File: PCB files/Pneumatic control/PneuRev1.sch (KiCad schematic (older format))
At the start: 5 parts

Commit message: 11/29 OpAmp switching
-Changed circuit from High side switch IC to opamp symbol
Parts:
- removed C?: C, symbol C
- removed R? (x3): R, symbol R
- removed U?: TPS1H000AQDGNRQ1, symbol TPS1H000AQDGNRQ1
- added R?: 1k, symbol R
- added R?: 100, symbol R
- added R?: 380, symbol R
- added U?: OP07, symbol OP07
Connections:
- net labels removed: +24V
- wire segments 15 -> 11
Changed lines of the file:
@@
 LIBS:contrib
 LIBS:valves
+LIBS:PneuRev1-cache
 EELAYER 25 0
 EELAYER END
@@
 $EndDescr
 $Comp
-L TPS1H000AQDGNRQ1 U?
-U 1 1 5BECF8AF
-P 6100 3725
-F 0 "U?" H 6100 3225 60  0000 C CNN
-F 1 "TPS1H000AQDGNRQ1" H 6100 4375 60  0000 C CNN
-F 2 "" H 6100 3725 60  0001 C CNN
-F 3 "" H 6100 3725 60  0001 C CNN
-	1    6100 3725
+L +5V #PWR?
+U 1 1 5BED02C0
+P 4375 2925
+F 0 "#PWR?" H 4375 2775 50  0001 C CNN
+F 1 "+5V" H 4375 3065 50  0000 C CNN
+F 2 "" H 4375 2925 50  0001 C CNN
+F 3 "" H 4375 2925 50  0001 C CNN
+	1    4375 2925
+	1    0    0    -1
+$EndComp
+$Comp
+L OP07 U?
+U 1 1 5C00B50F
+P 5600 3375
+F 0 "U?" H 5650 3625 50  0000 L CNN
+F 1 "OP07" H 5650 3525 50  0000 L CNN
+F 2 "" H 5650 3425 50  0001 C CNN
+F 3 "" H 5650 3525 50  0001 C CNN
+	1    5600 3375
+	1    0    0    -1
+$EndComp
+Wire Wire Line
+	4375 2925 4375 3275
+Wire Wire Line
+	4375 3275 5300 3275
+$Comp
+L R R?
+U 1 1 5C00B58E
+P 4375 3425
+F 0 "R?" V 4455 3425 50  0000 C CNN
+F 1 "1k" V 4375 3425 50  0000 C CNN
+F 2 "" V 4305 3425 50  0001 C CNN
+F 3 "" H 4375 3425 50  0001 C CNN
+	1    4375 3425
+	1    0    0    -1
+$EndComp
+$Comp
+L GND #PWR?
+U 1 1 5C00B5C1
+P 4375 3575
+F 0 "#PWR?" H 4375 3325 50  0001 C CNN
+F 1 "GND" H 4375 3425 50  0000 C CNN
+F 2 "" H 4375 3575 50  0001 C CNN
+F 3 "" H 4375 3575 50  0001 C CNN
+	1    4375 3575
+	1    0    0    -1
+$EndComp
+Wire Wire Line
+	5150 3475 5150 4025
+Wire Wire Line
+	5150 3475 5300 3475
+$Comp
+L R R?
+U 1 1 5C00B637
+P 5150 4175
+F 0 "R?" V 5230 4175 50  0000 C CNN
+F 1 "100" V 5150 4175 50  0000 C CNN
+F 2 "" V 5080 4175 50  0001 C CNN
+F 3 "" H 5150 4175 50  0001 C CNN
+	1    5150 4175
 	1    0    0    -1
 $EndComp
 $Comp
 L R R?
-U 1 1 5BECF8E3
-P 4675 3325
-F 0 "R?" V 4755 3325 50  0000 C CNN
-F 1 "R" V 4675 3325 50  0000 C CNN
-F 2 "" V 4605 3325 50  0001 C CNN
-F 3 "" H 4675 3325 50  0001 C CNN
-	1    4675 3325
+U 1 1 5C00B68B
+P 5550 3950
+F 0 "R?" V 5630 3950 50  0000 C CNN
+F 1 "380" V 5550 3950 50  0000 C CNN
+F 2 "" V 5480 3950 50  0001 C CNN
+F 3 "" H 5550 3950 50  0001 C CNN
+	1    5550 3950
 	0    1    1    0
 $EndComp
-$Comp
-L R R?
-U 1 1 5BECF983
-P 5050 4075
-F 0 "R?" V 5130 4075 50  0000 C CNN
-F 1 "R" V 5050 4075 50  0000 C CNN
-F 2 "" V 4980 4075 50  0001 C CNN
-F 3 "" H 5050 4075 50  0001 C CNN
-	1    5050 4075
-	0    1    1    0
-$EndComp
-$Comp
-L C C?
-U 1 1 5BECFA51
-P 6900 4075
-F 0 "C?" H 6925 4175 50  0000 L CNN
-F 1 "C" H 6925 3975 50  0000 L CNN
-F 2 "" H 6938 3925 50  0001 C CNN
-F 3 "" H 6900 4075 50  0001 C CNN
-	1    6900 4075
-	-1   0    0    1
-$EndComp
+Wire Wire Line
+	5150 3950 5400 3950
+Connection ~ 5150 3950
+Wire Wire Line
+	5700 3950 6050 3950
+Wire Wire Line
+	6050 3950 6050 3375
+Wire Wire Line
+	5900 3375 6750 3375
+Wire Wire Line
+	5500 3075 5500 2725
 $Comp
 L GND #PWR?
-U 1 1 5BECFB91
-P 6900 4475
-F 0 "#PWR?" H 6900 4225 50  0001 C CNN
-F 1 "GND" H 6900 4325 50  0000 C CNN
-F 2 "" H 6900 4475 50  0001 C CNN
-F 3 "" H 6900 4475 50  0001 C CNN
-	1    6900 4475
-	1    0    0    -1
-$EndComp
-$Comp
-L R R?
-U 1 1 5BECFDE5
-P 5025 3525
-F 0 "R?" V 5105 3525 50  0000 C CNN
-F 1 "R" V 5025 3525 50  0000 C CNN
-F 2 "" V 4955 3525 50  0001 C CNN
-F 3 "" H 5025 3525 50  0001 C CNN
-	1    5025 3525
-	-1   0    0    1
-$EndComp
-$Comp
-L GND #PWR?
-U 1 1 5BECFE76
-P 5025 3675
-F 0 "#PWR?" H 5025 3425 50  0001 C CNN
-F 1 "GND" H 5025 3525 50  0000 C CNN
-F 2 "" H 5025 3675 50  0001 C CNN
-F 3 "" H 5025 3675 50  0001 C CNN
-	1    5025 3675
-	1    0    0    -1
-$EndComp
-$Comp
-L +24V #PWR?
-U 1 1 5BED01EB
-P 6900 3050
-F 0 "#PWR?" H 6900 2900 50  0001 C CNN
-F 1 "+24V" H 6900 3190 50  0000 C CNN
-F 2 "" H 6900 3050 50  0001 C CNN
-F 3 "" H 6900 3050 50  0001 C CNN
-	1    6900 3050
+U 1 1 5C00B76C
+P 5500 3700
+F 0 "#PWR?" H 5500 3450 50  0001 C CNN
+F 1 "GND" H 5500 3550 50  0000 C CNN
+F 2 "" H 5500 3700 50  0001 C CNN
+F 3 "" H 5500 3700 50  0001 C CNN
+	1    5500 3700
 	1    0    0    -1
 $EndComp
 Wire Wire Line
-	4825 3325 5550 3325
-Wire Wire Line
-	5200 3925 5550 3925
-Wire Wire Line
-	6650 3925 6900 3925
-Wire Wire Line
-	6900 4225 6900 4475
-Wire Wire Line
-	5025 3375 5025 3325
-Connection ~ 5025 3325
-Wire Wire Line
-	5200 3925 5200 4075
-Wire Wire Line
-	6900 3050 6900 3325
-Wire Wire Line
-	6900 3325 6650 3325
+	5500 3675 5500 3700
 $Comp
-L +5V #PWR?
-U 1 1 5BED02C0
-P 4125 3125
-F 0 "#PWR?" H 4125 2975 50  0001 C CNN
-F 1 "+5V" H 4125 3265 50  0000 C CNN
-F 2 "" H 4125 3125 50  0001 C CNN
-F 3 "" H 4125 3125 50  0001 C CNN
-	1    4125 3125
+L GND #PWR?
+U 1 1 5C00B92E
+P 5150 4525
+F 0 "#PWR?" H 5150 4275 50  0001 C CNN
+F 1 "GND" H 5150 4375 50  0000 C CNN
+F 2 "" H 5150 4525 50  0001 C CNN
+F 3 "" H 5150 4525 50  0001 C CNN
+	1    5150 4525
 	1    0    0    -1
 $EndComp
 Wire Wire Line
-	4125 3125 4125 3325
-Wire Wire Line
-	4125 3325 4525 3325
-Wire Wire Line
-	6650 3725 7200 3725
-Wire Wire Line
-	7200 3725 7200 4425
-Wire Wire Line
-	7200 4425 6900 4425
-Connection ~ 6900 4425
-$Comp
-L GND #PWR?
-U 1 1 5BED065C
-P 4775 4500
-F 0 "#PWR?" H 4775 4250 50  0001 C CNN
-F 1 "GND" H 4775 4350 50  0000 C CNN
-F 2 "" H 4775 4500 50  0001 C CNN
-F 3 "" H 4775 4500 50  0001 C CNN
-	1    4775 4500
-	1    0    0    -1
-$EndComp
-Wire Wire Line
-	4900 4075 4775 4075
-Wire Wire Line
-	4775 4075 4775 4500
+	5150 4325 5150 4525
+Connection ~ 6050 3375
 $EndSCHEMATC

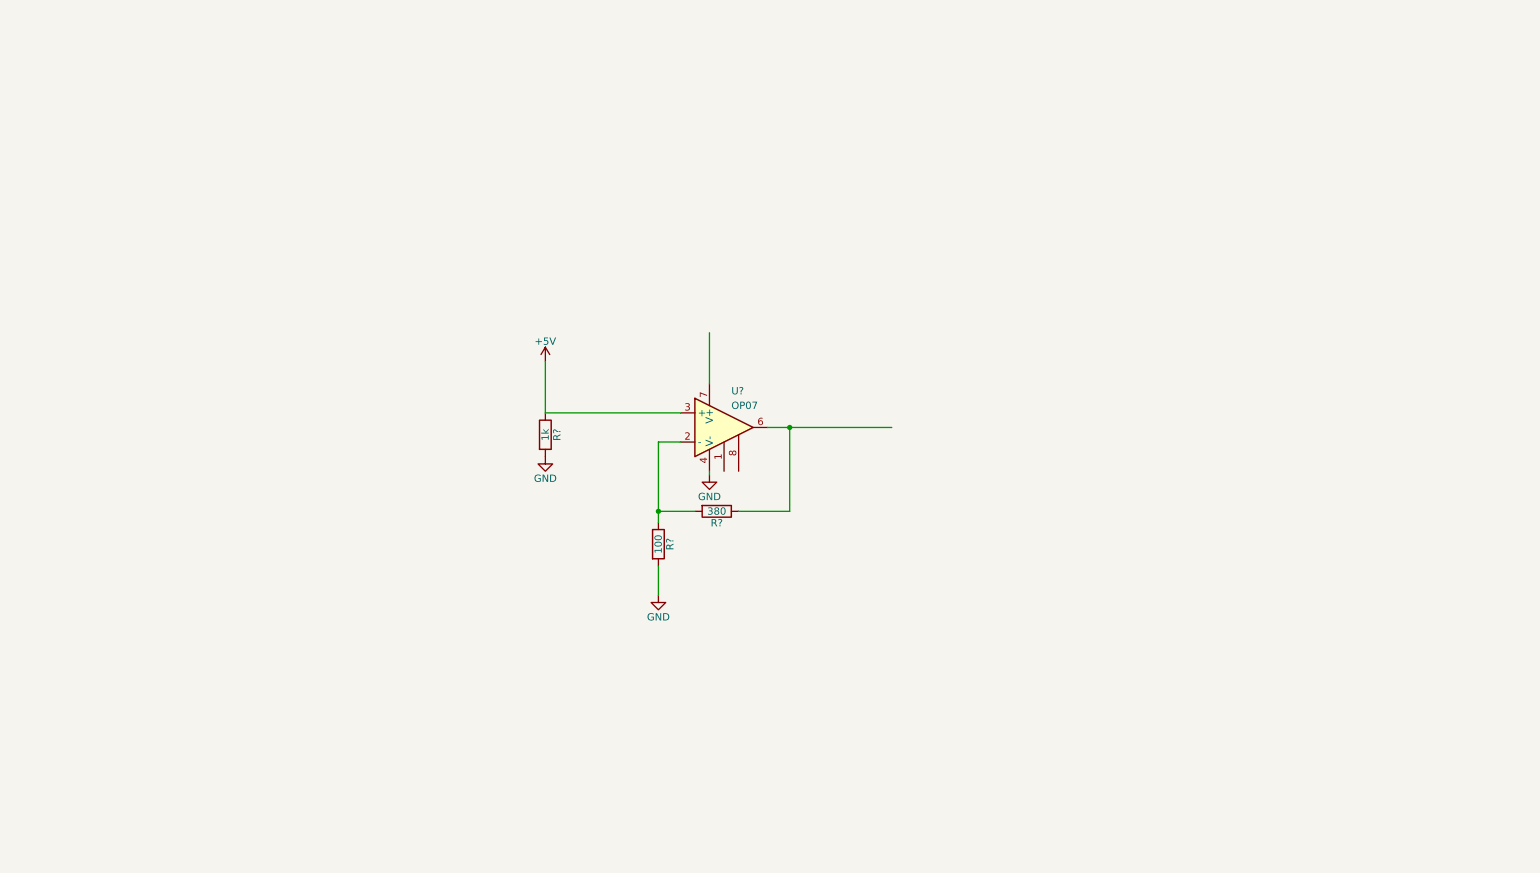
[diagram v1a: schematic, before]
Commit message: 11/30/2018
-Added bus lines
-Added net names for in/out
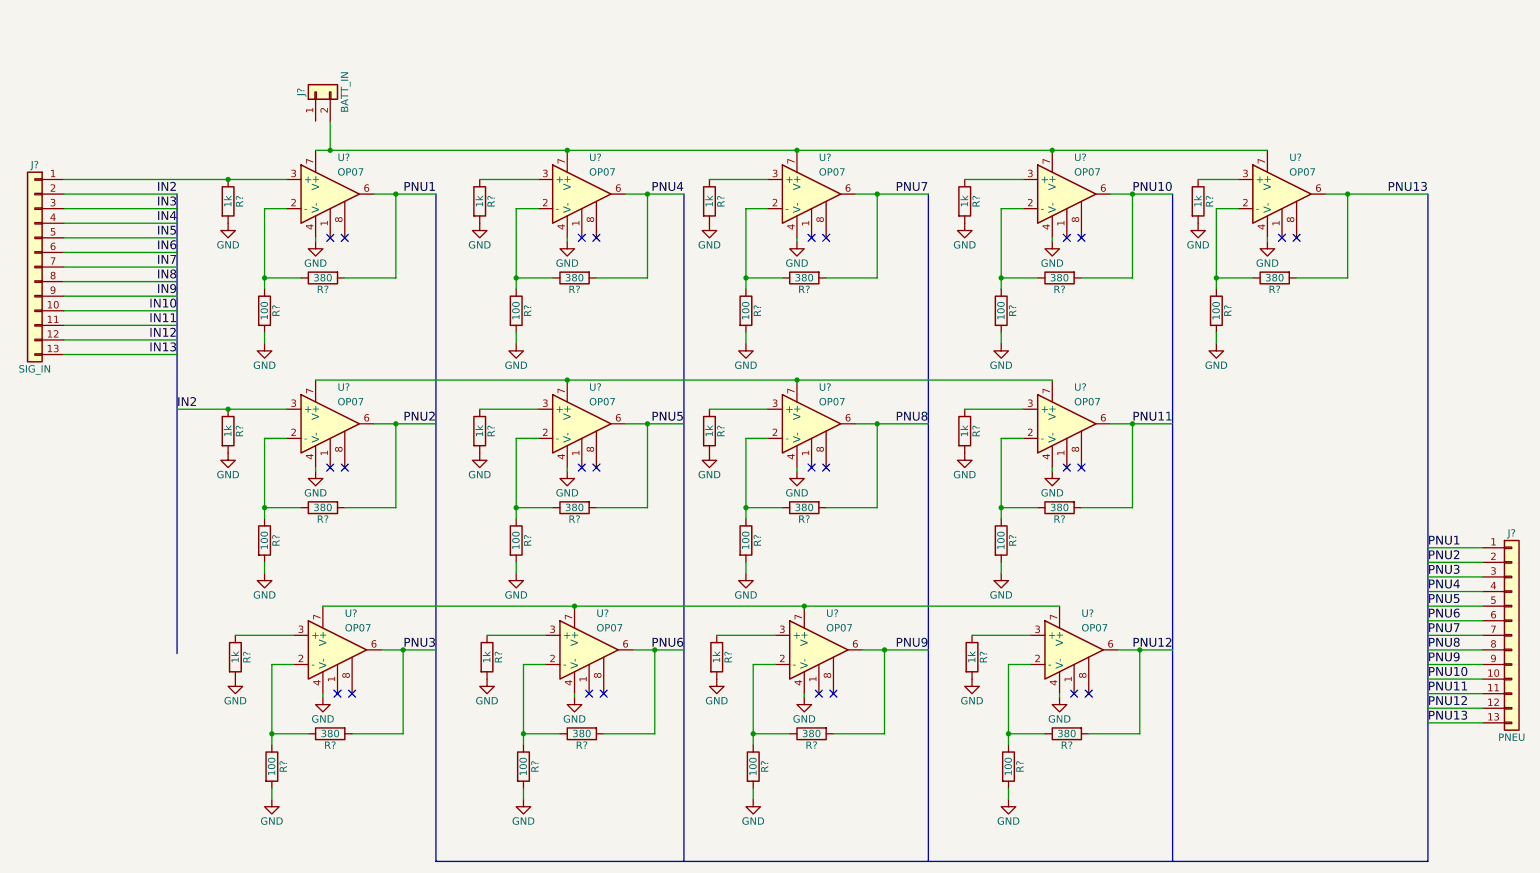
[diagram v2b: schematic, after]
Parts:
- added J?: SIG_IN, symbol Conn_01x13
- added J?: PNEU, symbol Conn_01x13
- added J?: BATT_IN, symbol Conn_01x02
- added R? (x12): 1k, symbol R
- added R? (x12): 100, symbol R
- added R? (x12): 380, symbol R
- added U? (x12): OP07, symbol OP07
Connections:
- net labels added: IN10, IN11, IN12, IN13, IN2, IN3, IN4, IN5, IN6, IN7, IN8, IN9, PNU1, PNU10, PNU11, PNU12, PNU13, PNU2, PNU3, PNU4, PNU5, PNU6, PNU7, PNU8, PNU9
- net labels removed: +5V
- wire segments 11 -> 182
- no-connect marks 0 -> 26
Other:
- moved on the sheet: R?, U?

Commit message: 12/5/2018
-Changed to dual op amps
-Added ua78 regulator
-finished schematic wiring
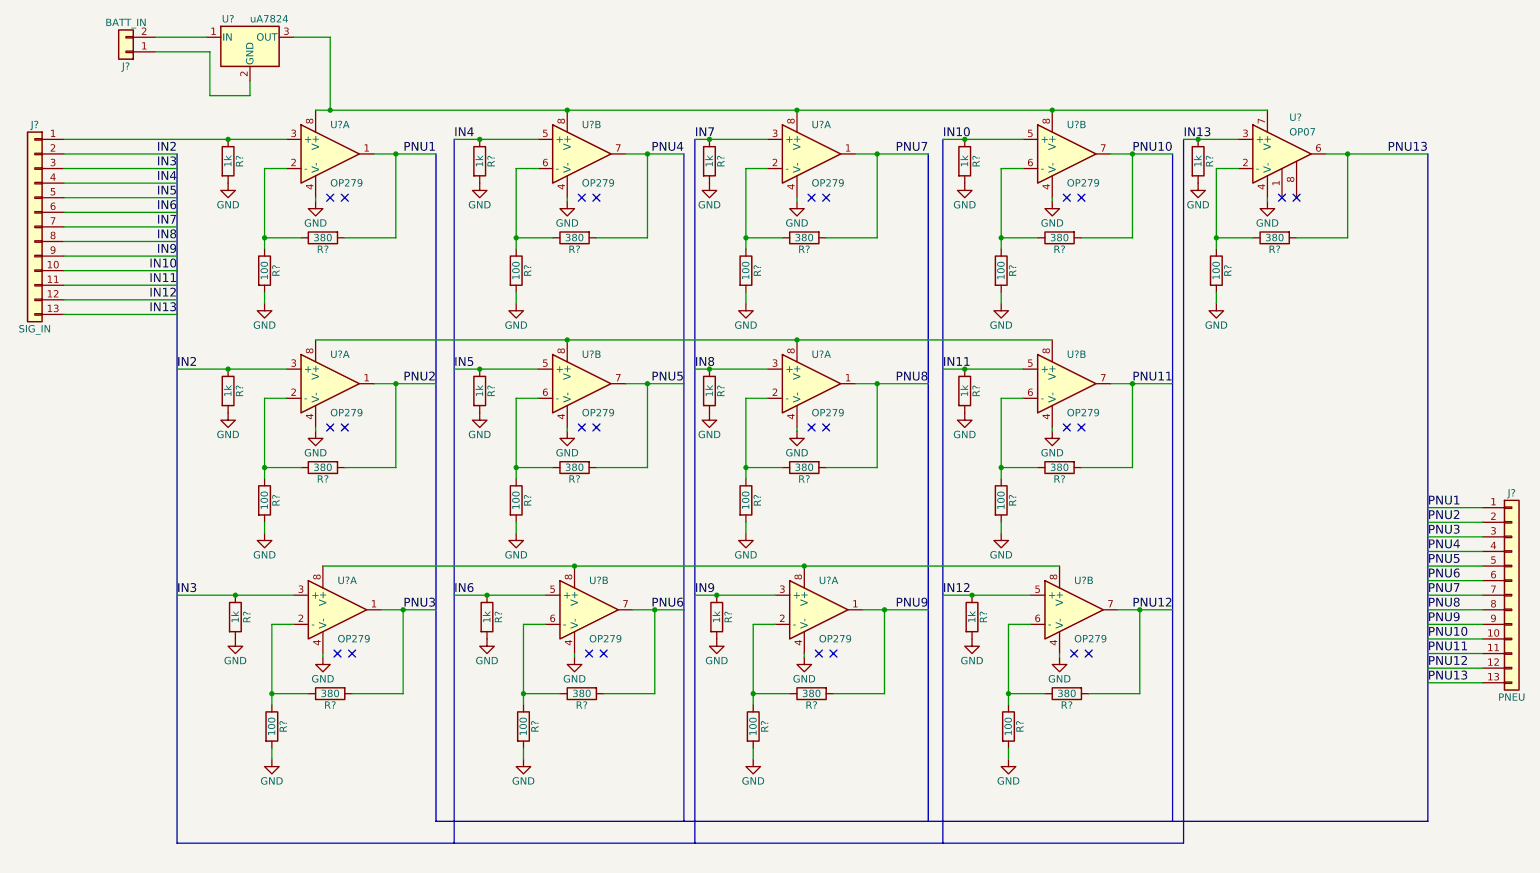
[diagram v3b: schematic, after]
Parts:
- removed U? (x12): OP07, symbol OP07
- added U? (x12): OP279, symbol OP279
- added U?: uA7824, symbol uA7824
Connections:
- net GND: now also U?.4 (V-), U?.4 (V-), U?.4 (V-), U?.4 (V-), U?.4 (V-), U?.4 (V-), U?.4 (V-), U?.4 (V-), U?.4 (V-), U?.4 (V-), U?.4 (V-), U?.4 (V-)
- net IN10: now also R?.1, U?.5 (+)
- net IN11: now also R?.1, U?.5 (+)
- net IN12: now also R?.1, U?.5 (+)
- net IN13: now also R?.1, U?.3 (+)
- net IN2: now also U?.3 (+)
- net IN3: now also R?.1, U?.3 (+)
- net IN4: now also R?.1, U?.5 (+)
- net IN5: now also R?.1, U?.5 (+)
- net IN6: now also R?.1, U?.5 (+)
- net IN7: now also R?.1, U?.3 (+)
- net IN8: now also R?.1, U?.3 (+)
- net IN9: now also R?.1, U?.3 (+)
- net PNU1: now also U?.1
- net PNU10: now also U?.7
- net PNU11: now also U?.7
- net PNU12: now also U?.7
- net PNU2: now also U?.1
- net PNU3: now also U?.1
- net PNU4: now also U?.7
- net PNU5: now also U?.7
- net PNU6: now also U?.7
- net PNU7: now also U?.1
- net PNU8: now also U?.1
- net PNU9: now also U?.1
- net at R?.1, R?.1: now also U?.2 (-) (x6)
- net at J?.1 (Pin_1), R?.1: now also U?.3 (+)
- net at J?.2 (Pin_2): now also U?.1 (IN); no longer U?.7 (V+)
- net at J?.1 (Pin_1): now also U?.2 (GND)
- net at R?.1, R?.1: now also U?.6 (-) (x6)
- new net: U?.3 (OUT), U?.7 (V+), U?.8 (V+), U?.8 (V+), U?.8 (V+), U?.8 (V+)
- new net: U?.8 (V+), U?.8 (V+), U?.8 (V+), U?.8 (V+) (x2)
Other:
- moved on the sheet: J?, R?, U?

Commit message: minor changes
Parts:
- gave numbers to parts that had none: 50
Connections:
- net IN11: now also U7.3 (+); no longer U7.5 (+)
- net IN2: now also U2.5 (+); no longer U2.3 (+)
- net IN5: now also U4.3 (+); no longer U4.5 (+)
- net IN8: now also U5.5 (+); no longer U5.3 (+)
- net PNU11: now also U7.1; no longer U7.7
- net PNU2: now also U2.7; no longer U2.1
- net PNU5: now also U4.1; no longer U4.7
- net PNU8: now also U5.7; no longer U5.1
- net at R5.1, R8.1: now also U2.6 (-); no longer U2.2 (-)
- net at R14.1, R17.1: now also U4.2 (-); no longer U4.6 (-)
- net at R23.1, R26.1: now also U5.6 (-); no longer U5.2 (-)
- net at R32.1, R35.1: now also U7.2 (-); no longer U7.6 (-)

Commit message: 1/20/2019
-Added all footprints
-Began PCB layout
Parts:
- J1, J3: footprint (none) -> Pin_Headers:Pin_Header_Straight_1x13_Pitch2.00mm
- J2: footprint (none) -> Connectors_Molex:Molex_KK-6410-02_02x2.54mm_Straight
- R1, R10, R11, R12, R13, R14, R15, R16, R17, R18, R19, R2, R20, R21, R22, R23, R24, R25, R26, R27, R28, R29, R3, R30, R31, R32, R33, R34, R35, R36, R37, R38, R39, R4, R5, R6, R7, R8, R9: footprint (none) -> Resistors_THT:R_Axial_DIN0204_L3.6mm_D1.6mm_P5.08mm_Horizontal
- U1: footprint (none) -> ua7824:TO254P1651X1067X470-3
- U2, U3, U4, U5, U6, U7, U8: footprint (none) -> dualopamp:SOIC127P600X175-8N

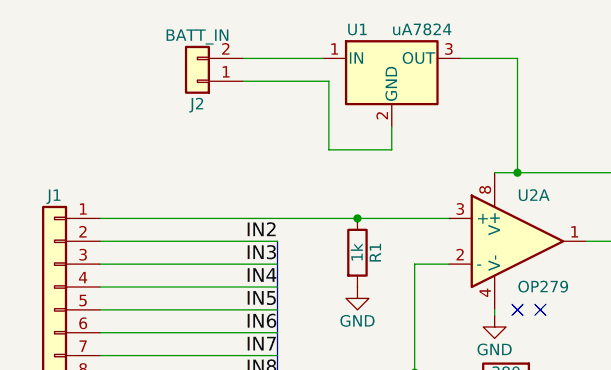
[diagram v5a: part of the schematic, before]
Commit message: 1/31/2019
-Added battery power indicator LED
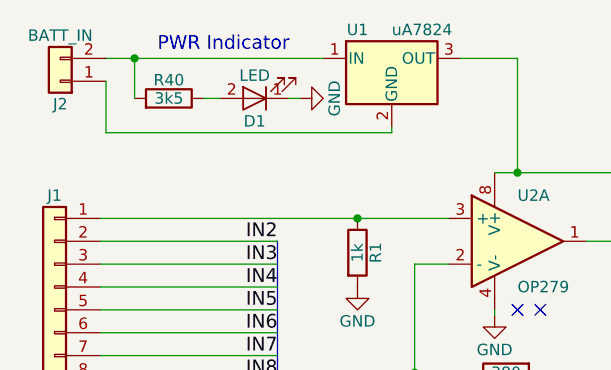
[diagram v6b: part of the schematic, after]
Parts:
- added D1: LED, LEDs:LED_D3.0mm, symbol LED
- added R40: 3k5, Resistors_THT:R_Axial_DIN0204_L3.6mm_D1.6mm_P5.08mm_Horizontal, symbol R
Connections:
- net GND: now also D1.1 (K)
- net at J2.2 (Pin_2), U1.1 (IN): now also R40.2
- new net: D1.2 (A), R40.1
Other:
- note added: "PWR Indicator"
- moved on the sheet: J2
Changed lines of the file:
@@
 L Conn_01x02 J2
 U 1 1 5C020053
-P 1500 800
-F 0 "J2" H 1500 900 50  0000 C CNN
-F 1 "BATT_IN" H 1500 600 50  0000 C CNN
-F 2 "Connectors_Molex:Molex_KK-6410-02_02x2.54mm_Straight" H 1500 800 50  0001 C CNN
-F 3 "" H 1500 800 50  0001 C CNN
-	1    1500 800
+P 900 800
+F 0 "J2" H 900 900 50  0000 C CNN
+F 1 "BATT_IN" H 900 600 50  0000 C CNN
+F 2 "Connectors_Molex:Molex_KK-6410-02_02x2.54mm_Straight" H 900 800 50  0001 C CNN
+F 3 "" H 900 800 50  0001 C CNN
+	1    900  800
 	-1   0    0    1
 $EndComp
@@
 $EndComp
 Wire Wire Line
-	2050 700  1700 700
-Wire Wire Line
-	1700 800  2075 800
-Wire Wire Line
-	2075 800  2075 1100
-Wire Wire Line
-	2075 1100 2350 1100
-Wire Wire Line
-	2350 1100 2350 1000
+	2350 1025 2350 1000
 Wire Wire Line
 	2650 700  2900 700
@@
 Text Label 8750 1400 0    60   ~ 0
 IN13
+$Comp
+L R R40
+U 1 1 5C537FB4
+P 1375 875
+F 0 "R40" V 1455 875 50  0000 C CNN
+F 1 "3k5" V 1375 875 50  0000 C CNN
+F 2 "Resistors_THT:R_Axial_DIN0204_L3.6mm_D1.6mm_P5.08mm_Horizontal" V 1305 875 50  0001 C CNN
+F 3 "" H 1375 875 50  0001 C CNN
+	1    1375 875
+	0    1    -1   0
+$EndComp
+$Comp
+L LED D1
+U 1 1 5C538514
+P 1750 875
+F 0 "D1" H 1750 975 50  0000 C CNN
+F 1 "LED" H 1750 775 50  0000 C CNN
+F 2 "LEDs:LED_D3.0mm" H 1750 875 50  0001 C CNN
+F 3 "" H 1750 875 50  0001 C CNN
+	1    1750 875
+	-1   0    0    1
+$EndComp
+Text Notes 1325 675  0    60   ~ 0
+PWR Indicator
+Wire Wire Line
+	2350 1025 1100 1025
+Wire Wire Line
+	1100 1025 1100 800
+Wire Wire Line
+	1600 875  1525 875
+Wire Wire Line
+	1225 875  1225 700
+Wire Wire Line
+	1100 700  2050 700
+Connection ~ 1225 700
+$Comp
+L GND #PWR040
+U 1 1 5C53B4F9
+P 1950 875
+F 0 "#PWR040" H 1950 625 50  0001 C CNN
+F 1 "GND" H 1950 725 50  0000 C CNN
+F 2 "" H 1950 875 50  0001 C CNN
+F 3 "" H 1950 875 50  0001 C CNN
+	1    1950 875
+	0    -1   -1   0
+$EndComp
+Wire Wire Line
+	1950 875  1900 875
 $EndSCHEMATC

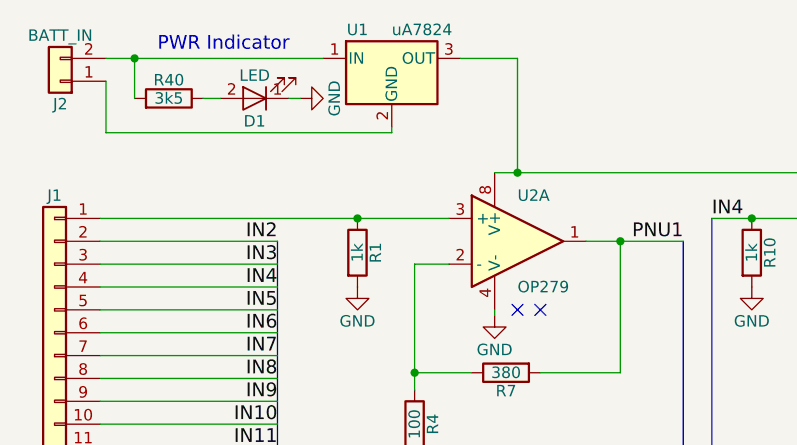
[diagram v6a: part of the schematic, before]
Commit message: 1/31/2019
-Gave board edge round corners
-Routed traces for PWR input part of the board
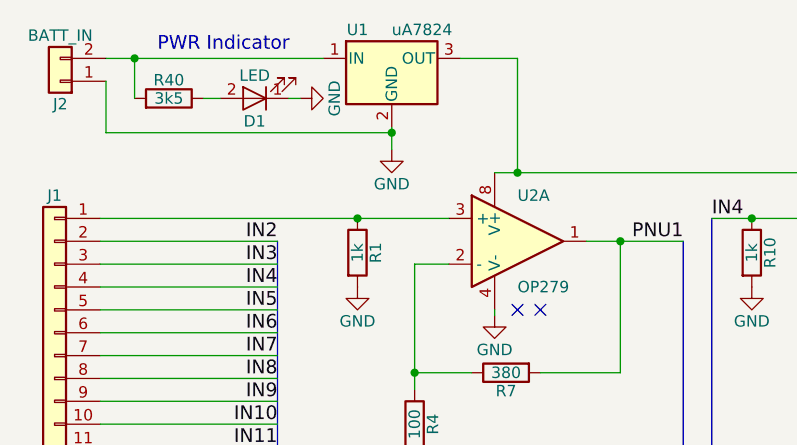
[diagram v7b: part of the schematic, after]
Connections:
- net GND: now also J2.1 (Pin_1), U1.2 (GND)
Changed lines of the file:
@@
 $EndComp
 Wire Wire Line
-	2350 1025 2350 1000
+	2350 1000 2350 1100
 Wire Wire Line
 	2650 700  2900 700
@@
 Wire Wire Line
 	1950 875  1900 875
+$Comp
+L GND #PWR?
+U 1 1 5C53AC5E
+P 2350 1100
+F 0 "#PWR?" H 2350 850 50  0001 C CNN
+F 1 "GND" H 2350 950 50  0000 C CNN
+F 2 "" H 2350 1100 50  0001 C CNN
+F 3 "" H 2350 1100 50  0001 C CNN
+	1    2350 1100
+	1    0    0    -1
+$EndComp
+Connection ~ 2350 1025
 $EndSCHEMATC
